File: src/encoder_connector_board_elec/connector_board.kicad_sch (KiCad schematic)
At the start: 5 parts, among them J1 Conn_02x12_Odd_Even, J2 Conn_01x06, J3 Conn_01x06, J4 Conn_01x06, J5 Conn_01x06

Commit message: Changes to footprint library
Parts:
- J2: footprint Connector_JST:JST_PH_B6B-PH-SM4-TB_1x06-1MP_P2.00mm_Vertical -> Bluesat:SM06B-PASS
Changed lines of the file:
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@@
 			)
 		)
-		(property "Footprint" "Connector_JST:JST_PH_B6B-PH-SM4-TB_1x06-1MP_P2.00mm_Vertical"
+		(property "Footprint" "Bluesat:SM06B-PASS"
 			(at 138.43 74.93 0)
 			(effects

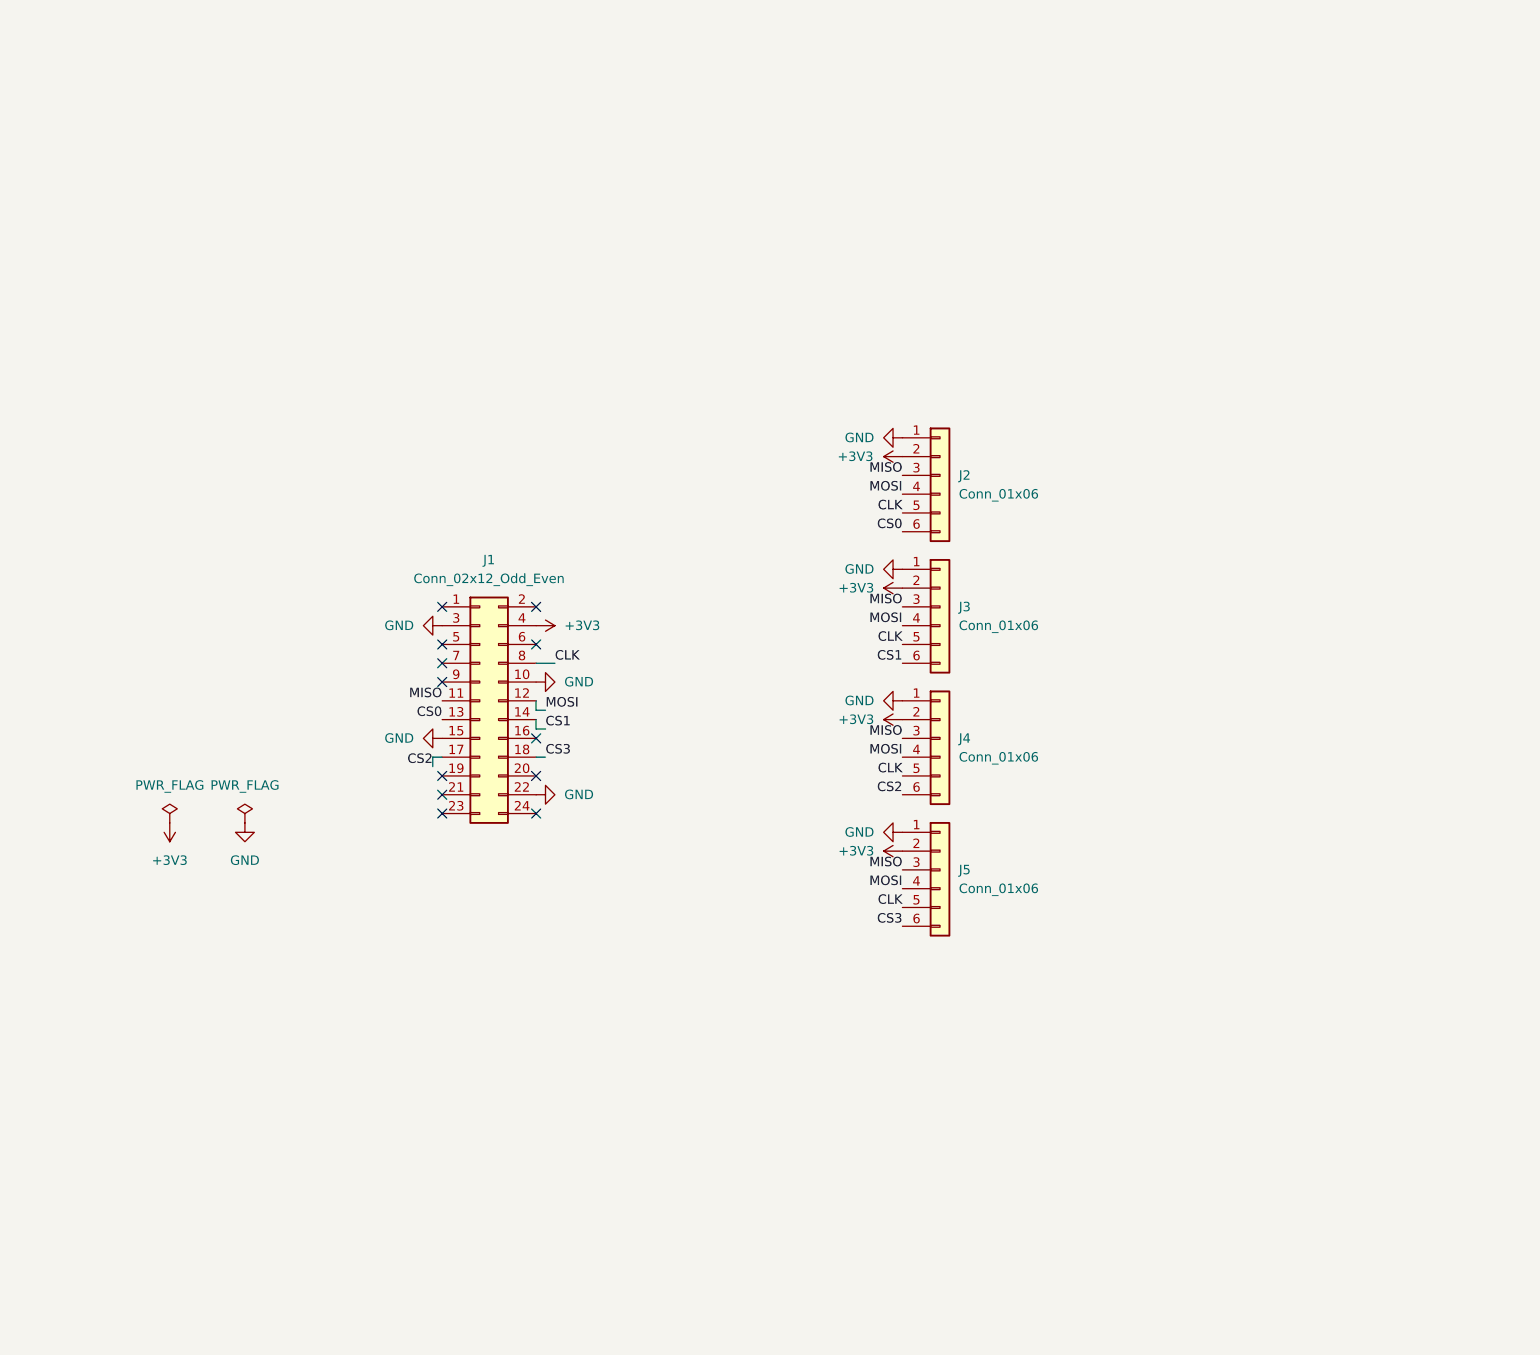
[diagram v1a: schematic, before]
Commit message: routing + change buck IC
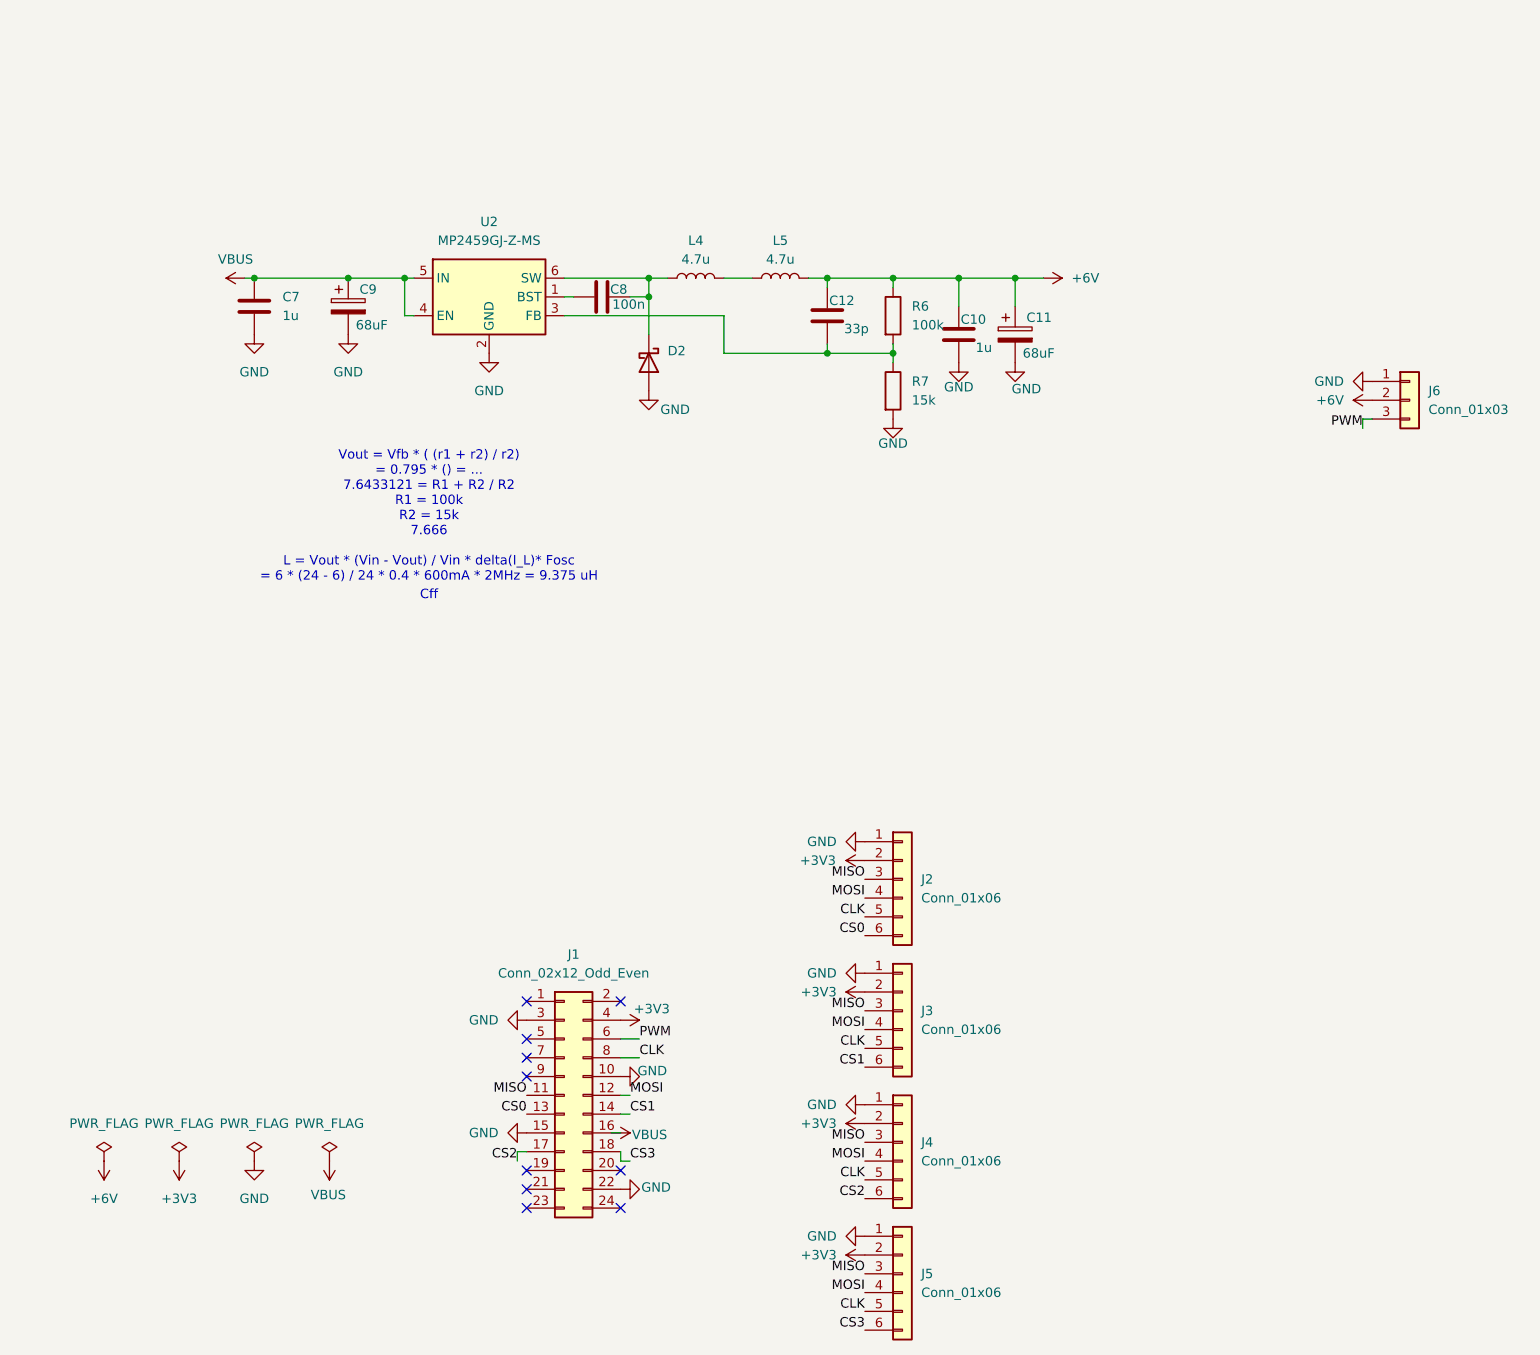
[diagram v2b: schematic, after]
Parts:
- added C10: 1u, Capacitor_SMD:C_0805_2012Metric, symbol Device:C
- added C11, C9: 68uF, Capacitor_SMD:CP_Elec_10x10, symbol Device:C_Polarized
- added C12: 33p, Capacitor_SMD:C_0402_1005Metric, symbol Device:C
- added C7: 1u, Capacitor_SMD:C_1206_3216Metric, symbol Device:C
- added C8: 100n, Capacitor_SMD:C_0402_1005Metric, symbol Device:C
- added D2: D_Schottky, Diode_SMD:D_SMA, symbol Device:D_Schottky
- added J6: Conn_01x03, Bluesat:BM03B-PASS, symbol Connector_Generic:Conn_01x03
- added L4, L5: 4.7u, Inductor_SMD:L_Changjiang_FNR4020S, symbol Device:L
- added R6: 100k, Resistor_SMD:R_0402_1005Metric, symbol Device:R
- added R7: 15k, Resistor_SMD:R_0402_1005Metric, symbol Device:R
- added U2: MP2459GJ-Z-MS, Package_TO_SOT_SMD:TSOT-23-6, symbol Bluesat:MP2459GJ-Z-MS
- J3, J4, J5: footprint Connector_JST:JST_PH_B6B-PH-SM4-TB_1x06-1MP_P2.00mm_Vertical -> Bluesat:SM06B-PASS
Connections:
- net GND: now also C10.2, C11.2, C7.2, C9.2, D2.2 (A), J6.1 (Pin_1), R7.2, U2.2 (GND)
- net VBUS: now reaches J1.16 (Pin_16)
- net VBUS: now also C7.1, C9.1, U2.4 (EN), U2.5 (IN)
- net PWM: now reaches J1.6 (Pin_6)
- net PWM: now also J6.3 (Pin_3)
- new net: L4.2, L5.1
- new net: C8.2, D2.1 (K), L4.1, U2.6 (SW)
- new net: C12.2, R6.2, R7.1, U2.3 (FB)
- new net: C8.1, U2.1 (BST)
- new net +6V: C10.1, C11.1, C12.1, J6.2 (Pin_2), L5.2, R6.1
- no-connect marks 12 -> 10
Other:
- note added: "Cff"
- note added: "Vout = Vfb * ( (r1 + r2) / r2) = 0.795 * () = ... 7.6433121 = R1 + R2 / R2 R1 = 100k R2 = 15k 7.666 L = Vout * (Vin - Vout) / Vin * delta(I_L)* Fosc = 6 * (24 - 6) / 24 * 0.4 * 600mA * 2MHz = 9.375 uH"
- moved on the sheet: J1, J2, J3, J4, J5

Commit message: change schematic to be correct with new power stage
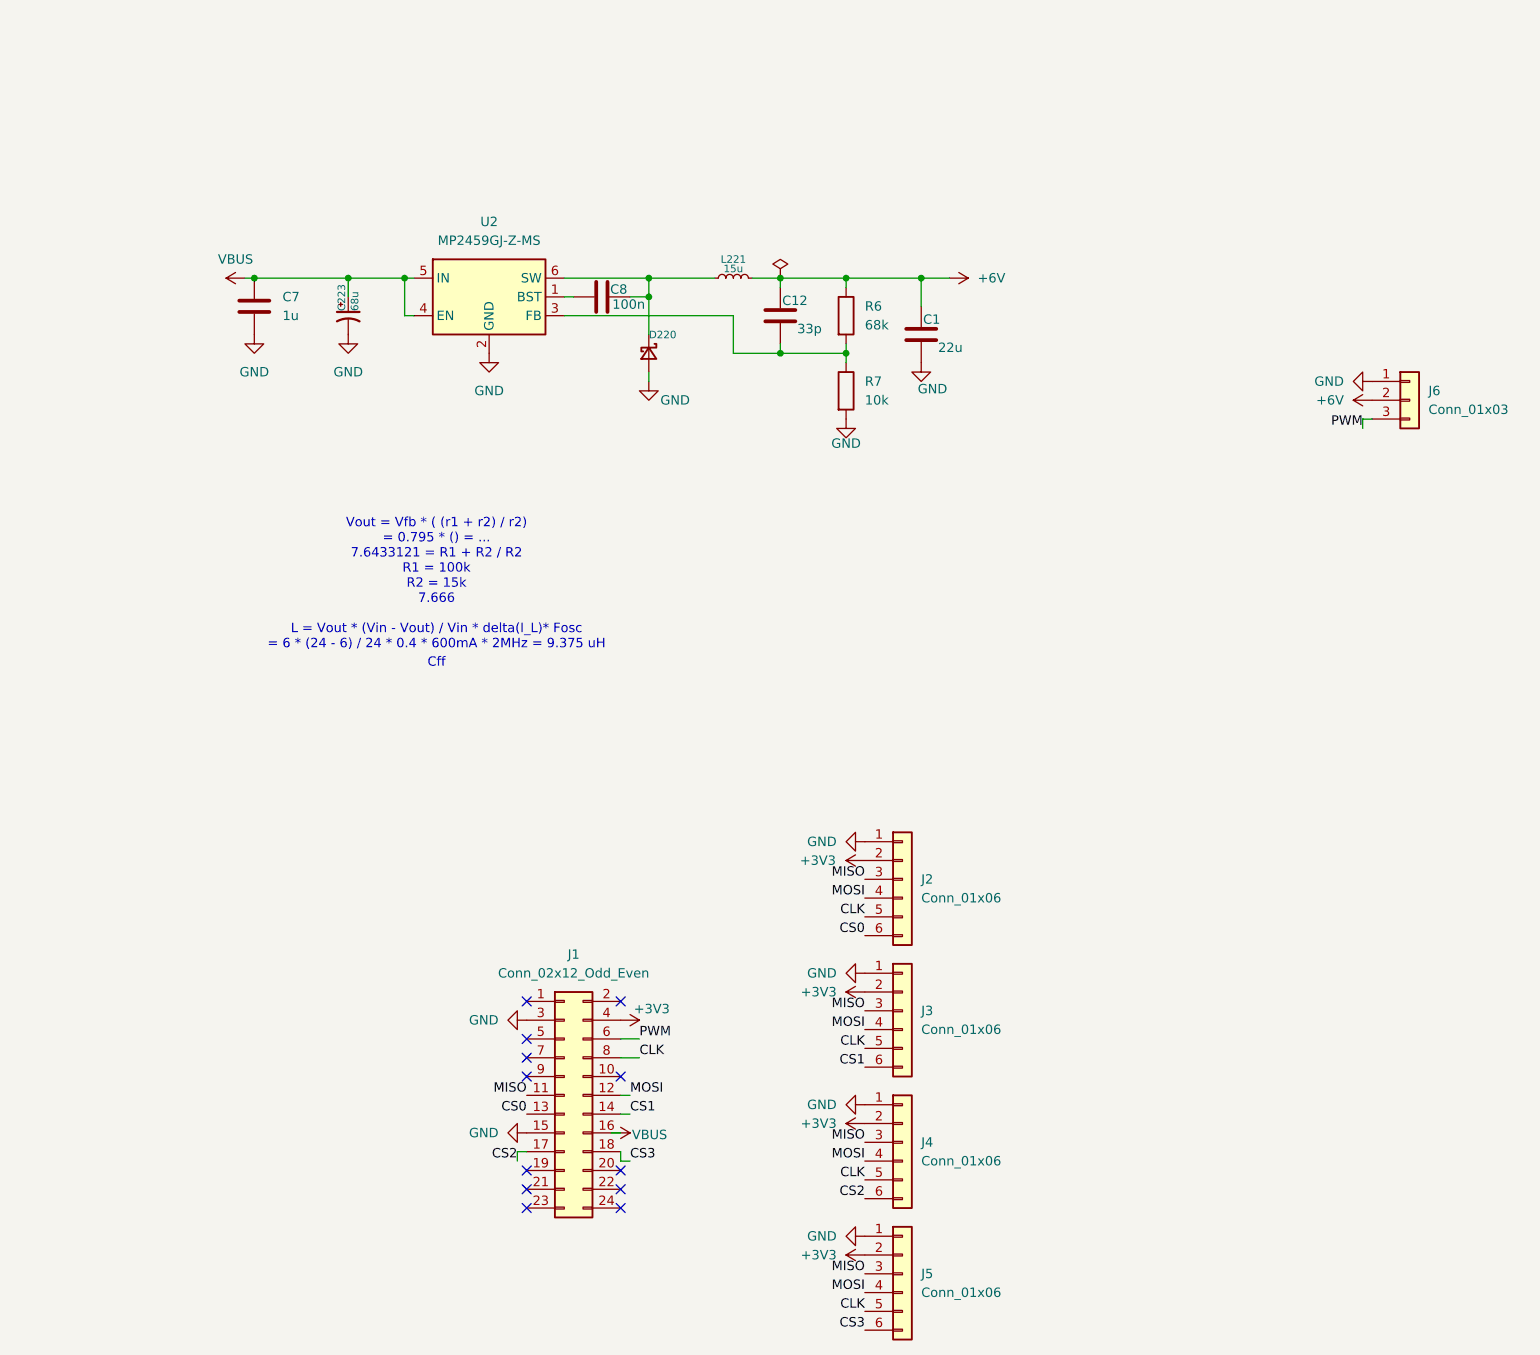
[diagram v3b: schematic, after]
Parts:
- removed C10: 1u, Capacitor_SMD:C_0805_2012Metric, symbol Device:C
- removed C11, C9: 68uF, Capacitor_SMD:CP_Elec_10x10, symbol Device:C_Polarized
- removed D2: D_Schottky, Diode_SMD:D_SMA, symbol Device:D_Schottky
- removed L4, L5: 4.7u, Inductor_SMD:L_Changjiang_FNR4020S, symbol Device:L
- added C1: 22u, Capacitor_SMD:C_1210_3225Metric, symbol Device:C
- added C223: 68u, Capacitor_SMD:CP_Elec_6.3x7.7, symbol Device:C_Polarized_Small_US
- added D220: D_Schottky_Small, Diode_SMD:D_SOD-123, symbol Device:D_Schottky_Small
- added L221: 15u, Inductor_SMD:L_Changjiang_FNR5040S, symbol Device:L_Small
- R6: value 100k -> 68k
- R7: value 15k -> 10k
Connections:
- net +6V: now also C1.1, L221.1
- net GND: now also C1.2, C223.2, D220.2 (A); no longer J1.10 (Pin_10), J1.22 (Pin_22)
- net VBUS: now also C223.1
- net at C8.2, U2.6 (SW): now also D220.1 (K), L221.2
- no-connect marks 10 -> 12
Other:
- moved on the sheet: C12, R6, R7

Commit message: Encoder connector board
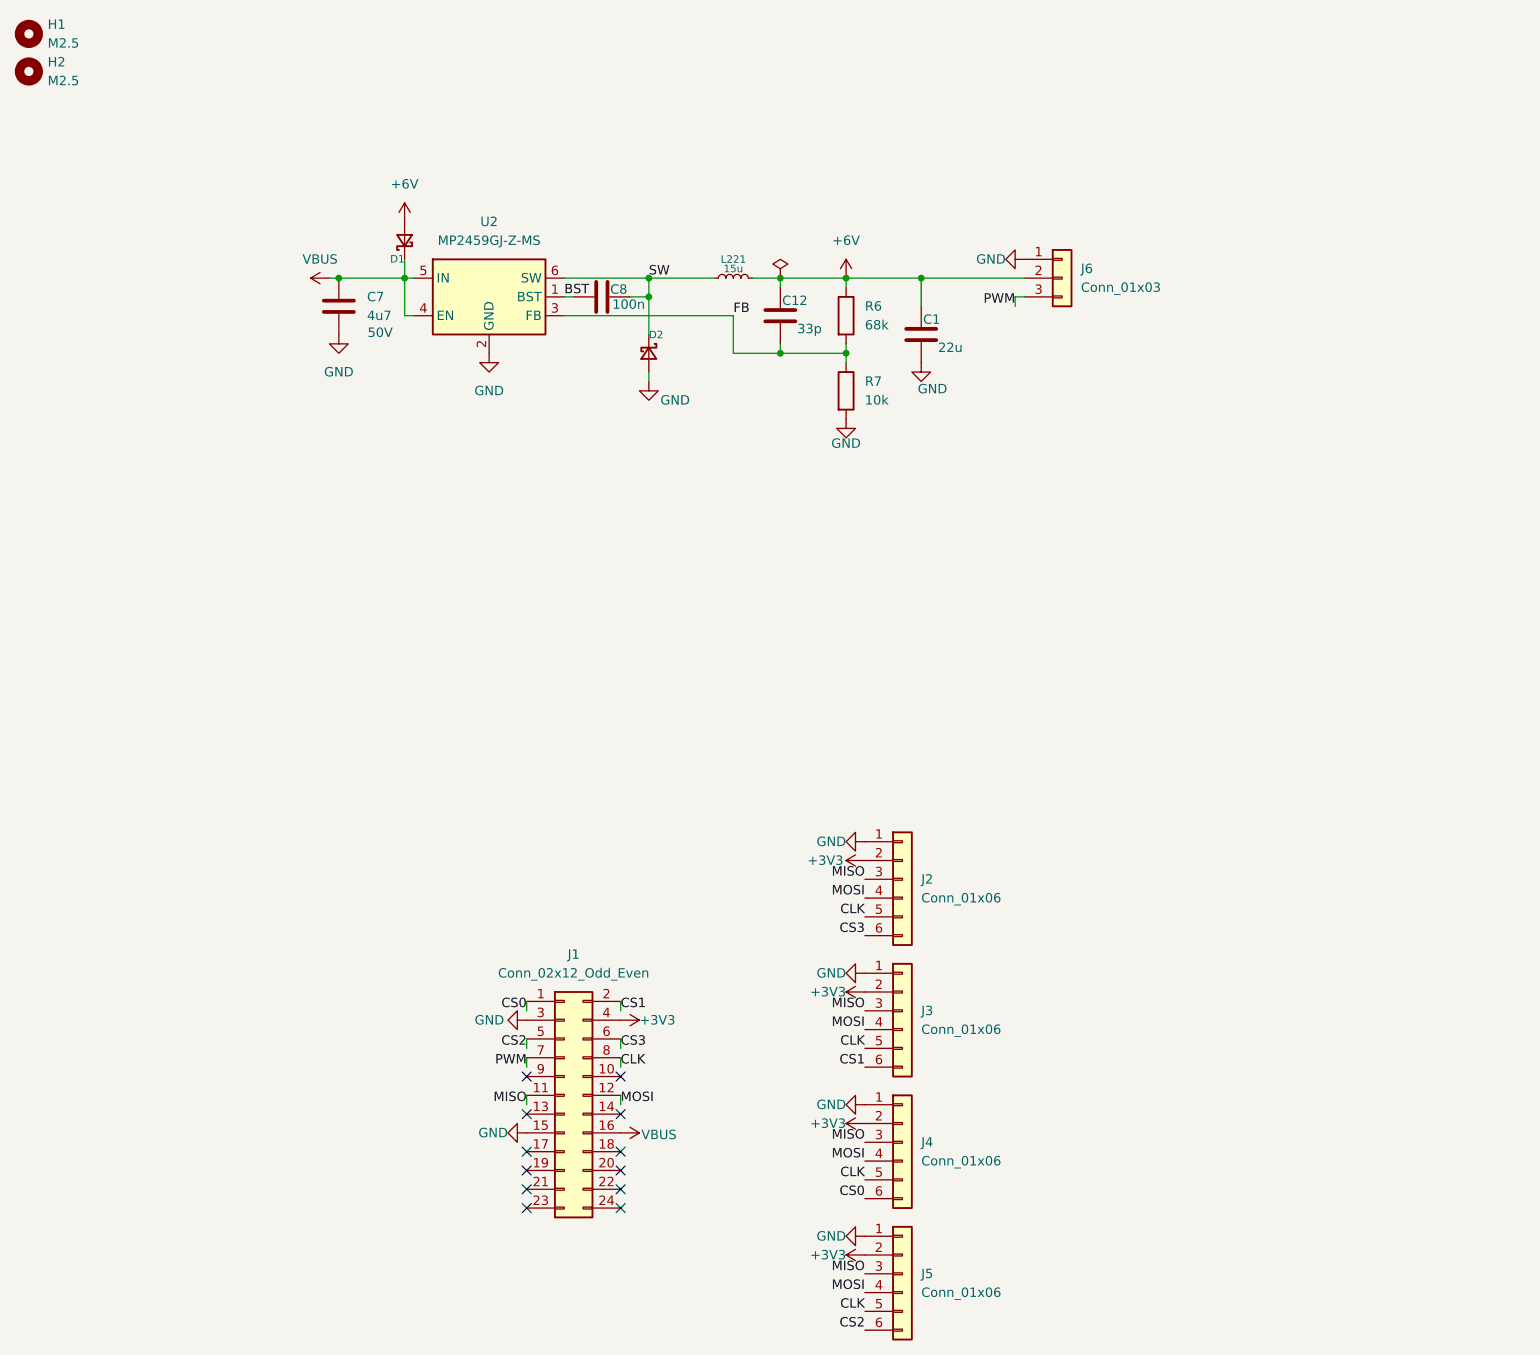
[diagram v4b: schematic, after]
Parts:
- removed C223: 68u, Capacitor_SMD:CP_Elec_6.3x7.7, symbol Device:C_Polarized_Small_US
- added D1: D_Schottky_Small, Diode_SMD:D_SOD-882, symbol Device:D_Schottky_Small
- added H1, H2: M2.5, Bluesat:M2.5_Internal, symbol Mechanical:MountingHole
- C7: value 1u -> 4u7; footprint Capacitor_SMD:C_1206_3216Metric -> Capacitor_SMD:C_1210_3225Metric; Rating (none) -> 50V
- J6: footprint Bluesat:BM03B-PASS -> Bluesat:SM03B-PASS
- renumbered D220 to D2
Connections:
- net +6V: now also D1.2 (A)
- net CS0: now also J1.1 (Pin_1), J4.6 (Pin_6); no longer J1.13 (Pin_13), J2.6 (Pin_6)
- net CS1: now also J1.2 (Pin_2); no longer J1.14 (Pin_14)
- net CS2: now also J1.5 (Pin_5), J5.6 (Pin_6); no longer J1.17 (Pin_17), J4.6 (Pin_6)
- net CS3: now also J1.6 (Pin_6), J2.6 (Pin_6); no longer J1.18 (Pin_18), J5.6 (Pin_6)
- net PWM: now also J1.7 (Pin_7); no longer J1.6 (Pin_6)
- net VBUS: now also D1.1 (K)
- net SW: now reaches C8.2, D2.1 (K), L221.2, U2.6 (SW)
- net FB: now reaches C12.2, R6.2, R7.1, U2.3 (FB)
- net BST: now reaches C8.1, U2.1 (BST)
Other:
- note removed: "Cff"
- note removed: "Vout = Vfb * ( (r1 + r2) / r2) = 0.795 * () = ... 7.6433121 = R1 + R2 / R2 R1 = 100k R2 = 15k 7.666 L = Vout * (Vin - Vout) / Vin * delta(I_L)* Fosc = 6 * (24 - 6) / 24 * 0.4 * 600mA * 2MHz = 9.375 uH"
- moved on the sheet: C7, J6
